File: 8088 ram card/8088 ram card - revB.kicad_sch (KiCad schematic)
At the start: 40 parts, among them J2 Conn_01x16_Socket, J3 Conn_01x16_Socket, P2 Conn_01x16_Pin, P3 Conn_01x16_Pin, Q1 2N3904, U1 4164, U10 74S04, U11 74S04, U12 74S00, U2 4164, U3 4164, U4 4164, U5 4164, U6 4164, U7 4164, U8 4164, U9 4164

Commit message: finished latest rev ram card version
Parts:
- C1: footprint (none) -> Evan's parts:noethstar tantalum
- C10, C11, C12, C13, C14, C2, C3, C4, C5, C6, C7, C8, C9: footprint (none) -> Evan's parts:northstar decoupling cap
- J2: footprint (none) -> Connector_PinSocket_2.54mm:PinSocket_1x16_P2.54mm_Vertical
- J3: footprint (none) -> Connector_PinSocket_2.54mm:PinSocket_1x18_P2.54mm_Vertical
- P2: footprint (none) -> Connector_PinHeader_2.54mm:PinHeader_1x16_P2.54mm_Vertical
- P3: footprint (none) -> Connector_PinHeader_2.54mm:PinHeader_1x18_P2.54mm_Vertical
- Q1: footprint Package_TO_SOT_THT:TO-92_Inline -> Evan's parts:TO-92_northstar_Wide
- R1, R2, R3, R4, R5, R6, R7: footprint (none) -> Evan's parts:northstar resistor
- RN1: footprint (none) -> Package_DIP:DIP-16_W7.62mm
- U1, U2, U3, U4, U5, U6, U7, U8, U9: footprint DIL16 -> Package_DIP:DIP-16_W7.62mm
- U10, U11, U12: footprint (none) -> Package_DIP:DIP-14_W7.62mm
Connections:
- net +5V: now also R2.2; no longer R2.1
- net at Q1.2 (B), R7.2: now also C2.1, R1.1; no longer C2.2, R1.2
- net at U12.9: now also R2.1; no longer R2.2
- new net: C2.2, R1.2, U12.8
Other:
- moved on the sheet: C2, R1

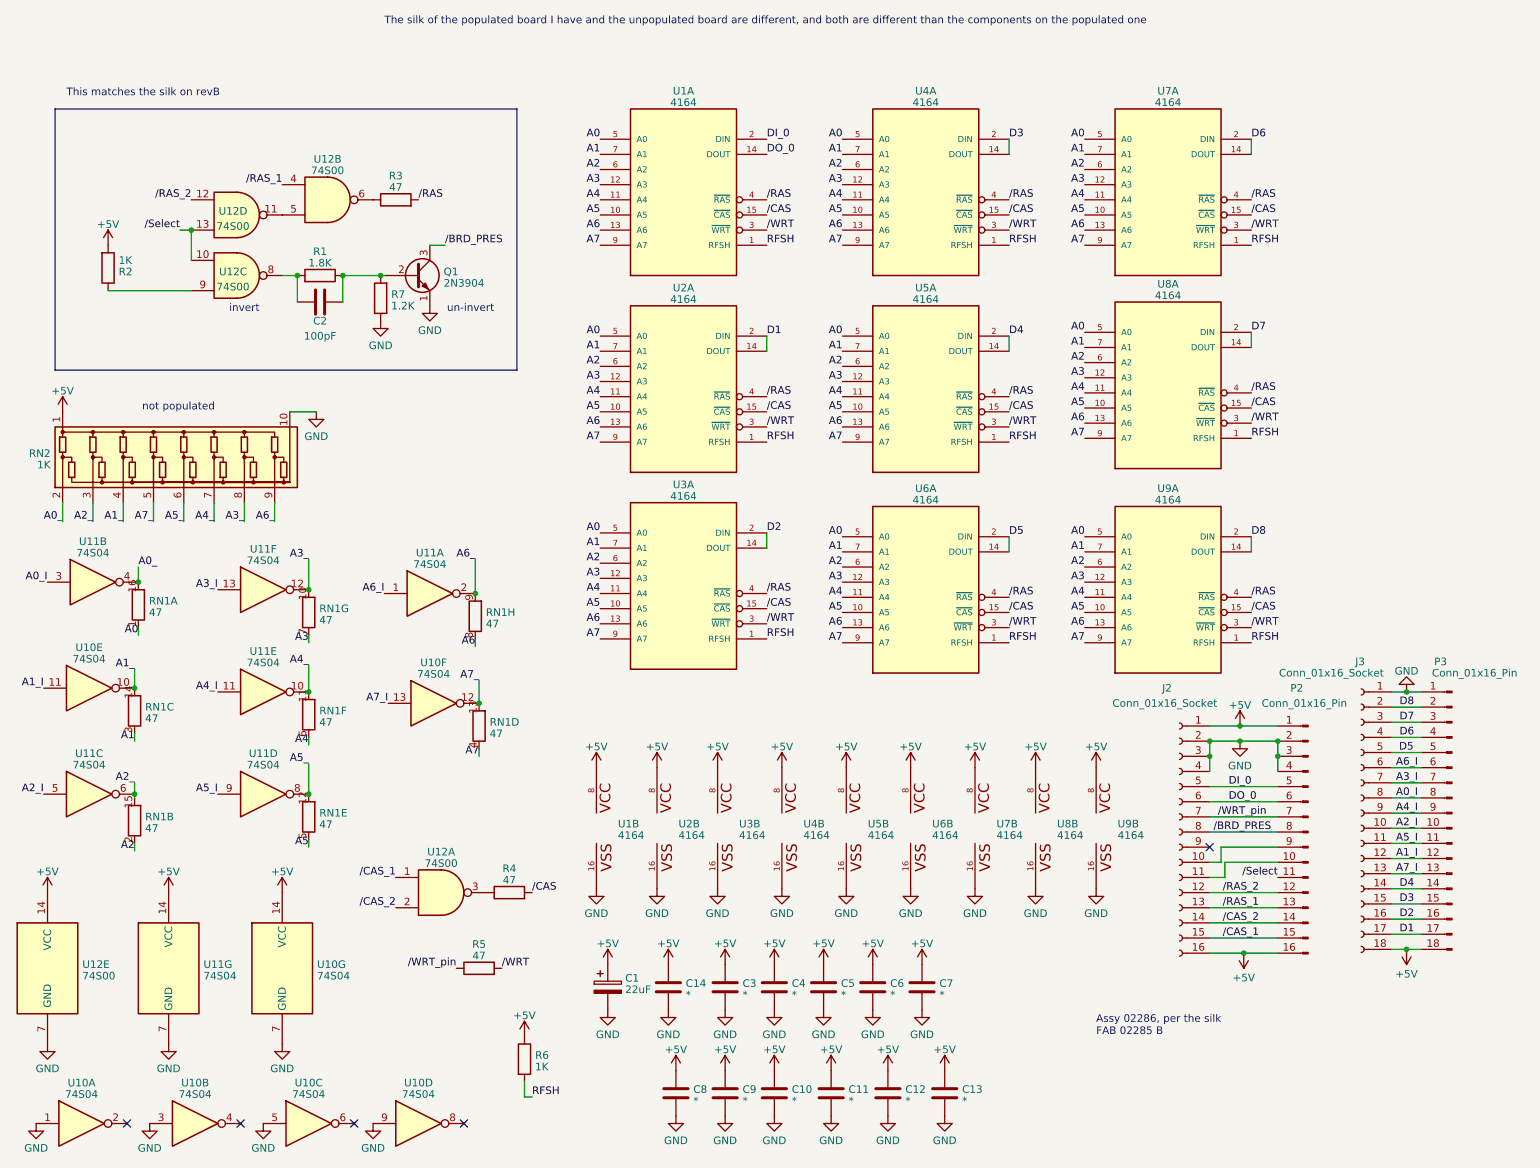
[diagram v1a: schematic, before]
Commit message: fixed reference designators for the one completed card
older revisions of the scheamtic not functionally wrong, but don't match the docs
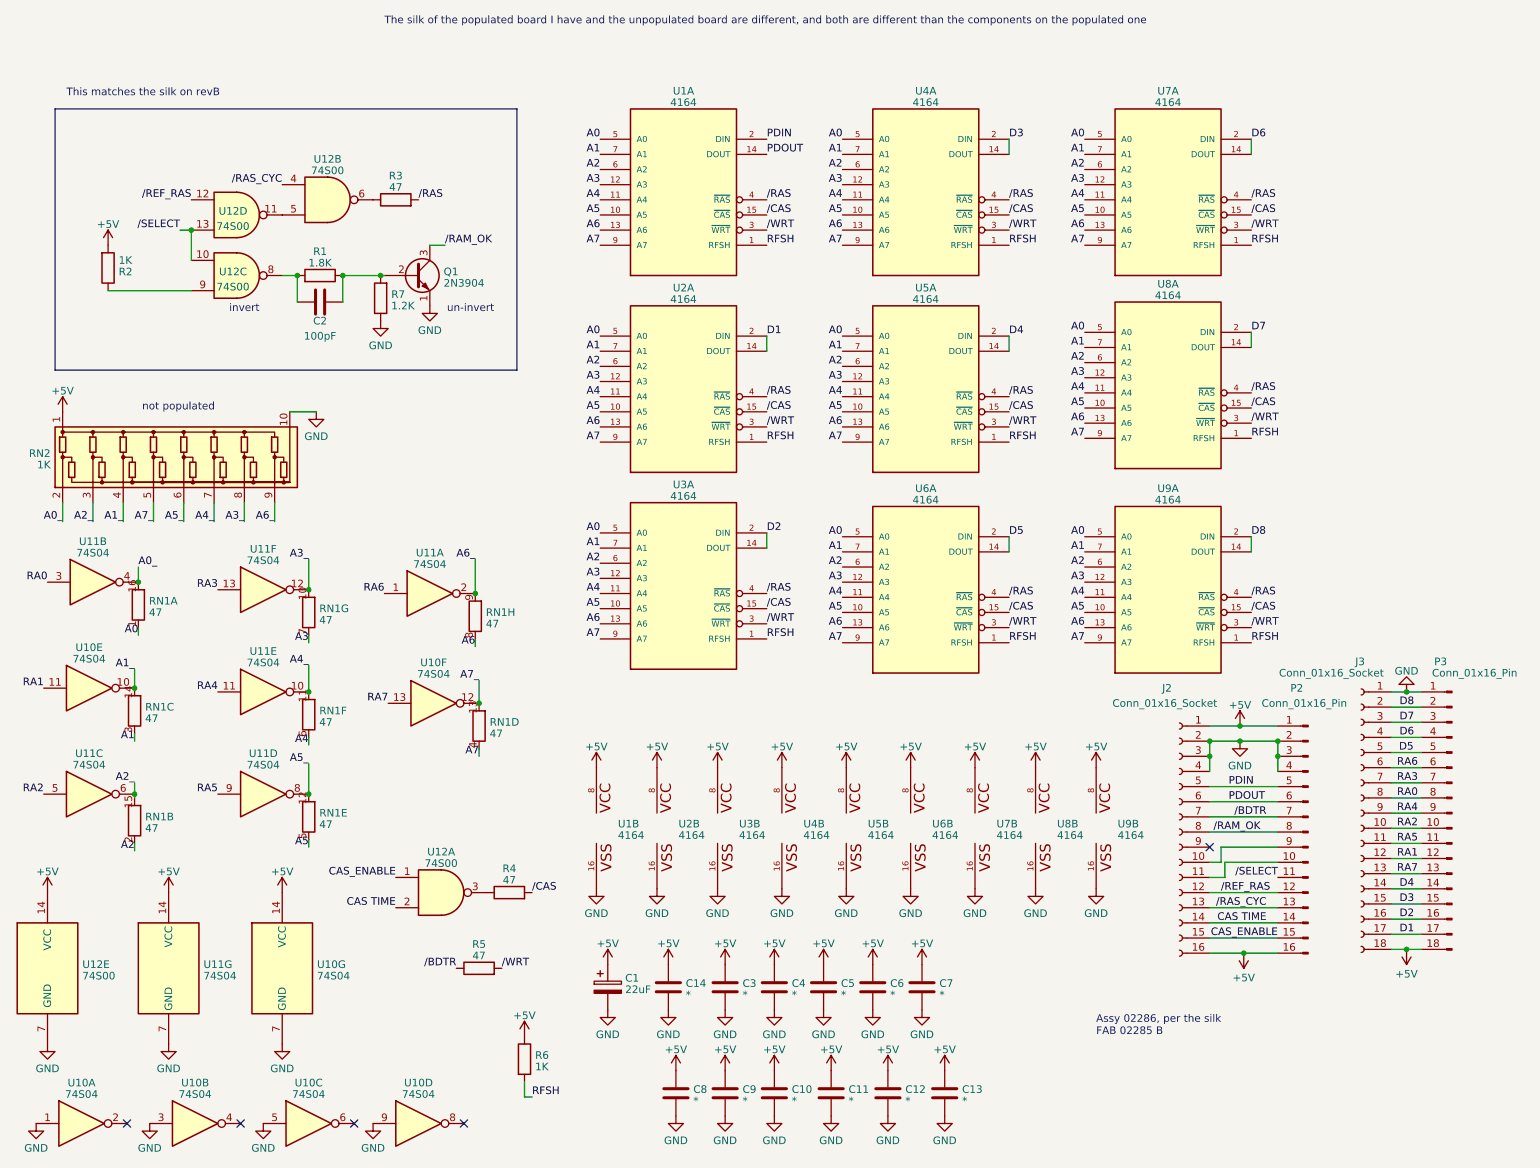
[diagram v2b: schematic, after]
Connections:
- net A0_I renamed RA0
- net A1_I renamed RA1
- net A2_I renamed RA2
- net A3_I renamed RA3
- net A4_I renamed RA4
- net A5_I renamed RA5
- net A6_I renamed RA6
- net A7_I renamed RA7
- net DI_0 renamed PDIN
- net DO_0 renamed PDOUT
- net /BRD_PRES renamed /RAM_OK
- net /CAS_1 renamed CAS_ENABLE
- net /CAS_2 renamed CAS TIME
- net /RAS_1 renamed /RAS_CYC
- net /RAS_2 renamed /REF_RAS
- net /Select renamed /SELECT
- net /WRT_pin renamed /BDTR
